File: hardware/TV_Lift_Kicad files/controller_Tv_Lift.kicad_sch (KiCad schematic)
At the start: 99 parts, among them J1 socket LAN8720a, J10 1844210, J11 1844223, J12 C5360899, J2 1836189, J3 1844223, J4 1844210, J5 1844223, J6 1844223, J7 1844236, J8 C5360899, J9 1844210, Q2 MMBT3906, SW1 TS-1187A-BAB, SW2 TS-1187A-BAB, SW3 TS-1187A-BAB, SW4 TS-1187A-BAB, U1 MAX3232, U10 VNH5019A-E, U2 TSOP32S40F, U3 SN65HVD230, U4 ESP32-WROOM-32, U5 LM2596S-5, U6 AMS1117-3.3, U7 PC817, U8 PC817, U9 b0505s-1we

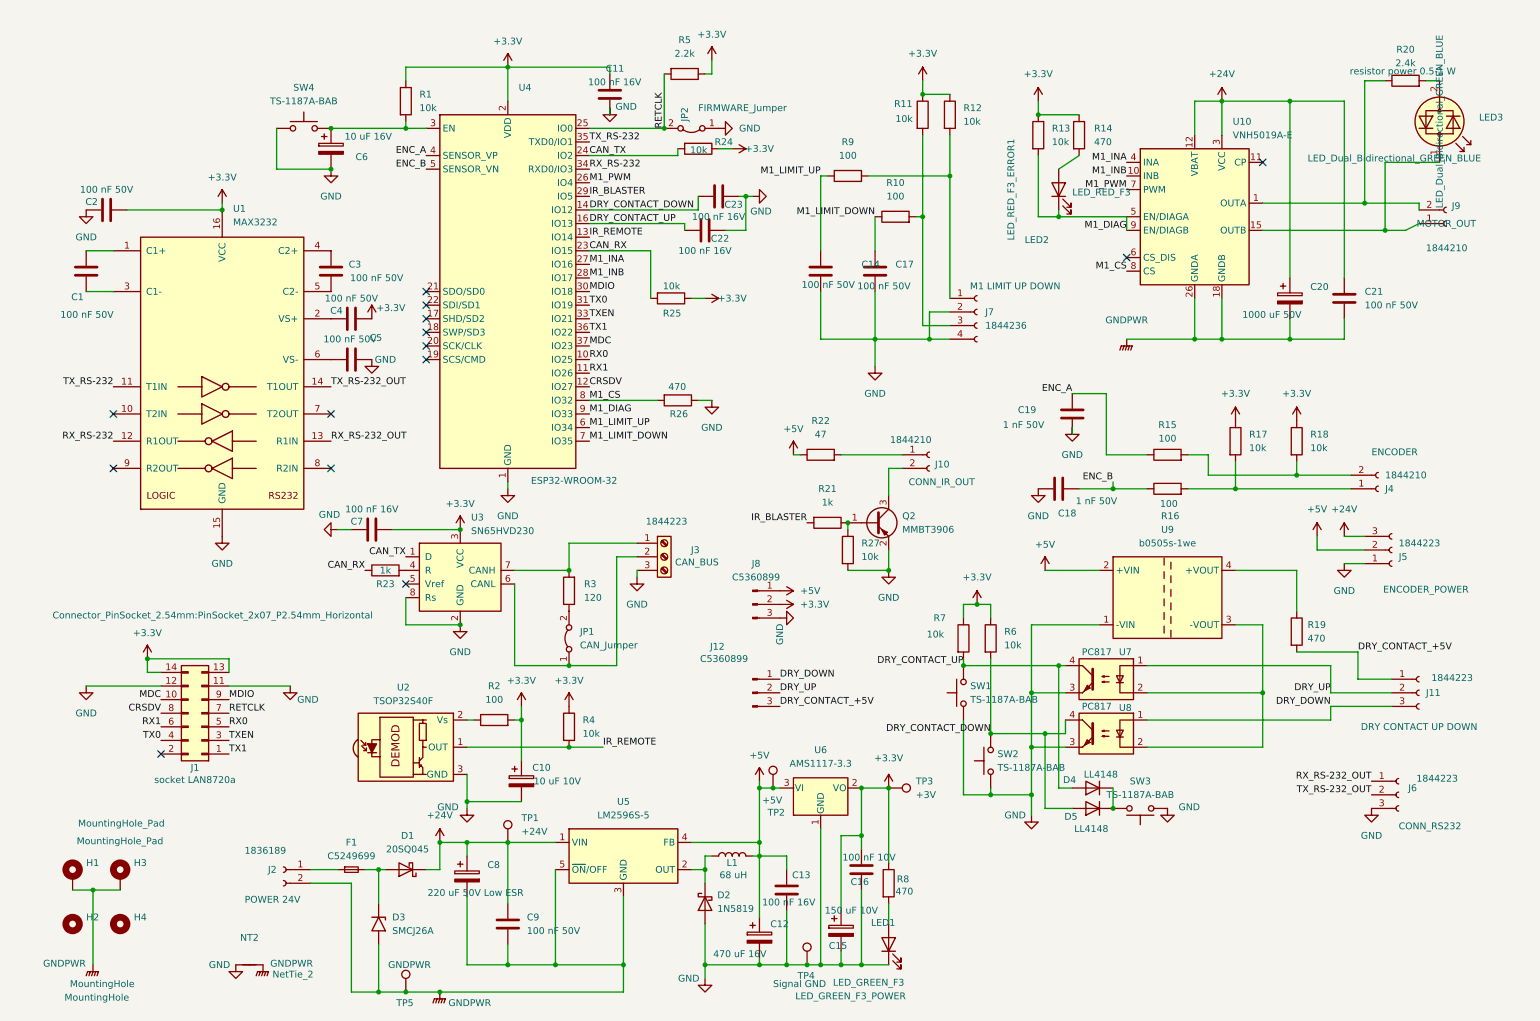
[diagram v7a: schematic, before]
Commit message: change capacitors on smd
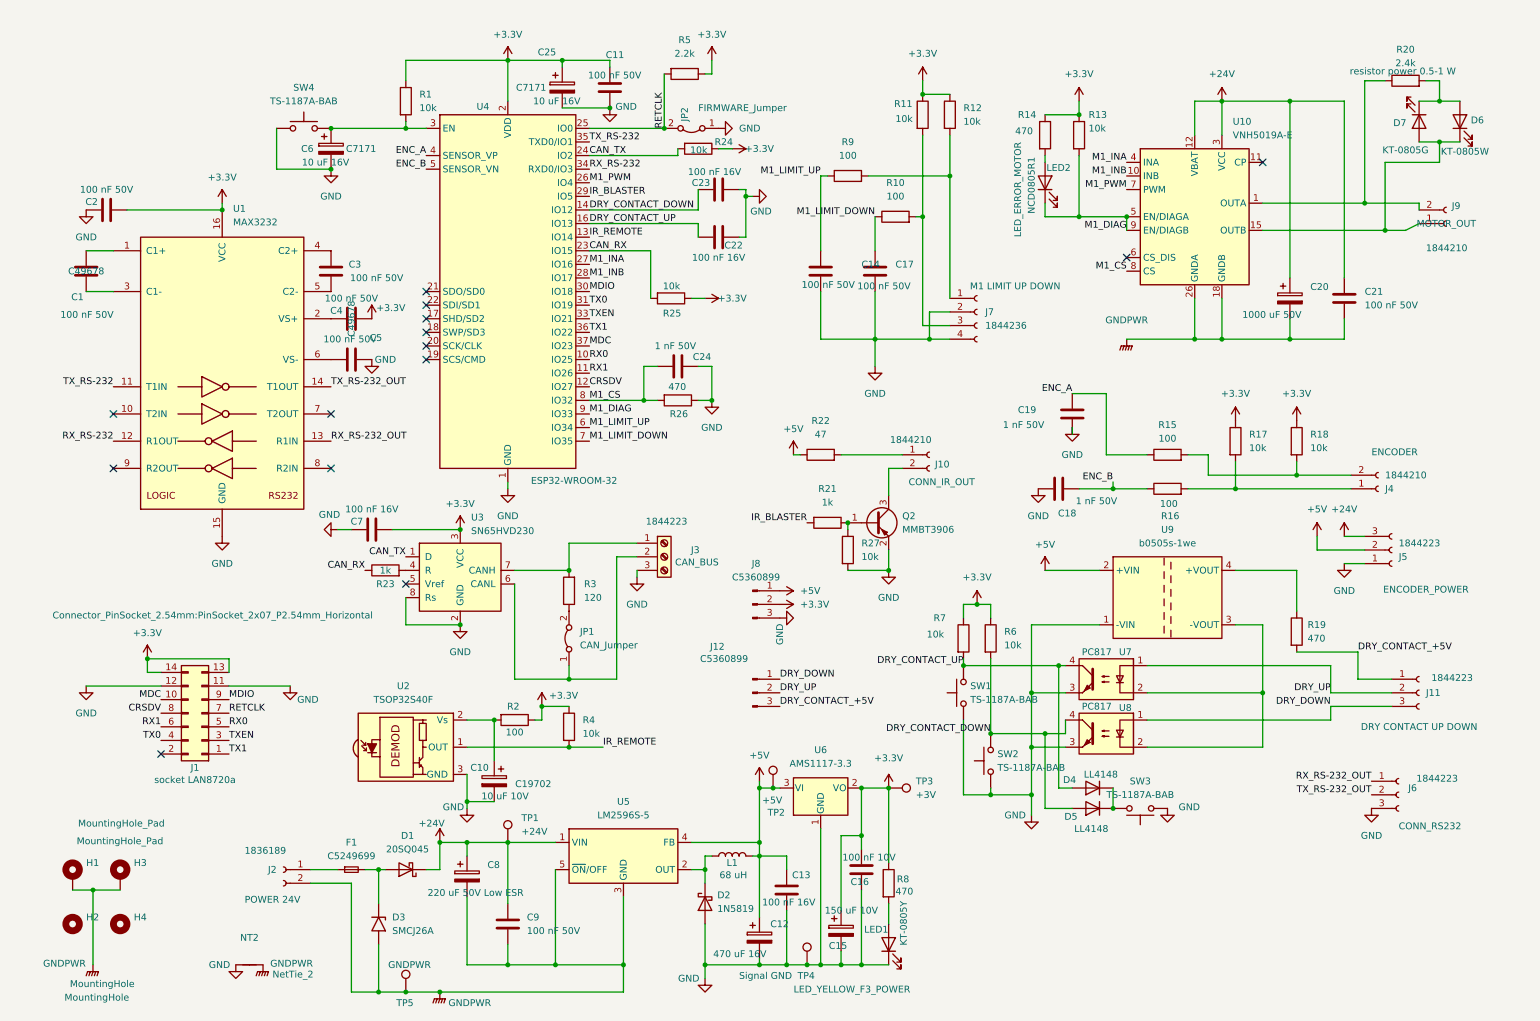
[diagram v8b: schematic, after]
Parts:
- removed LED3: LED_Dual_Bidirectional_GREEN_BLUE, LED_THT:LED_D3.0mm_Horizontal_O1.27mm_Z6.0mm, symbol Device:LED_Dual_Bidirectional
- added C24: 1 nF 50V, Capacitor_SMD:C_0805_2012Metric, symbol Device:C
- added C25: C7171, Capacitor_Tantalum_SMD:CP_EIA-3216-18_Kemet-A, symbol Device:C_Polarized
- added D6: KT-0805W, LED_SMD:LED_0805_2012Metric, symbol Device:LED
- added D7: KT-0805G, LED_SMD:LED_0805_2012Metric, symbol Device:LED
- C10: value 10 uF 10V -> C19702; footprint Capacitor_THT:CP_Radial_D5.0mm_P2.00mm -> Capacitor_SMD:C_0603_1608Metric
- C11: value 100 nF 16V -> 100 nF 50V
- C6: value 10 uF 16V -> C7171; footprint Capacitor_SMD:C_0805_2012Metric -> Capacitor_Tantalum_SMD:CP_EIA-3216-18_Kemet-A
- LED1: value LED_GREEN_F3 -> KT-0805Y; footprint LED_THT:LED_D3.0mm_Horizontal_O1.27mm_Z2.0mm -> LED_SMD:LED_0805_2012Metric
- LED2: value LED_RED_F3 -> NCD0805R1; footprint LED_THT:LED_D3.0mm_Horizontal_O1.27mm_Z6.0mm -> LED_SMD:LED_0805_2012Metric
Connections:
- net +3.3V: now also R2.1, C25.1; no longer C10.1, R2.2
- net GND: now also C24.1, C25.2
- net M1_CS: now also C24.2
- net at U2.2 (Vs): now also C10.1, R2.2; no longer R2.1
- net at R20.2: now also D6.2 (A), D7.1 (K)
- net at J9.1 (M+), U10.15 (OUTB), U10.16 (OUTB)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: now also D6.1 (K), D7.2 (A)
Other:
- moved on the sheet: C10, C11, C22, C23, LED2, R13, R14, R2
